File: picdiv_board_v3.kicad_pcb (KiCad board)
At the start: 2 copper layers, 75 x 100 mm, 81 parts, among them J1 DC-Input, J10 PPS_B, J101 MountingHole_M2.5, J102 Conn_Coaxial, J103 Conn_Coaxial, J104 MountingHole_M2.5, J105 Conn_01x06, J106 PPS_A, J107 PPS_A, J14 TEST_1PPS, J4 SYNC, J6 PPS_B, J8 SYNC, Q1 Q_PNP_BEC, Q2 Q_PNP_BEC, SW101 SW_DIP_x03, U101 LT1963AxT-3.3, U102 LT1963AxT-3.3, U103 LT1963AEQ, U104 LTC6993xS6-1, U105 IDT5PB1108, U3 PIC12F675, U6 IDT5PB1108

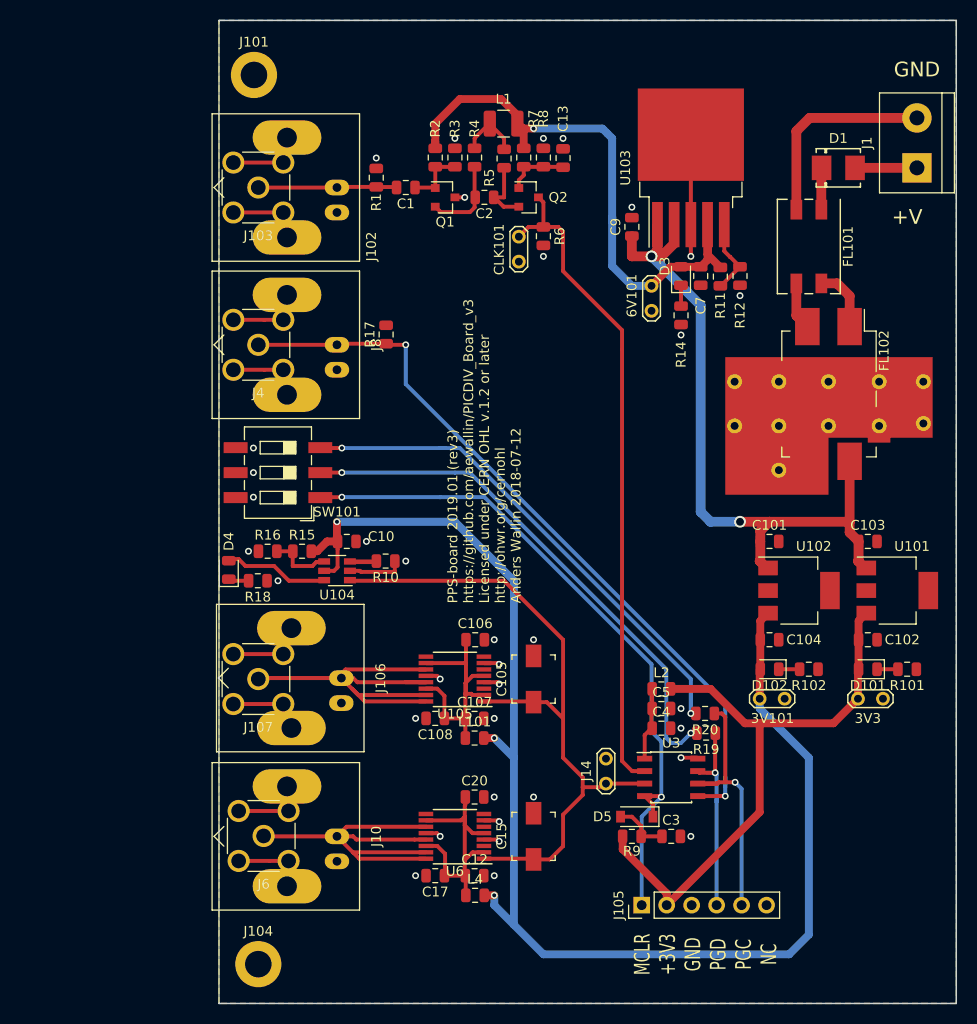
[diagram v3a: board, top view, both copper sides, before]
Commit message: gnd-vias, silk, move PPSB connectors.
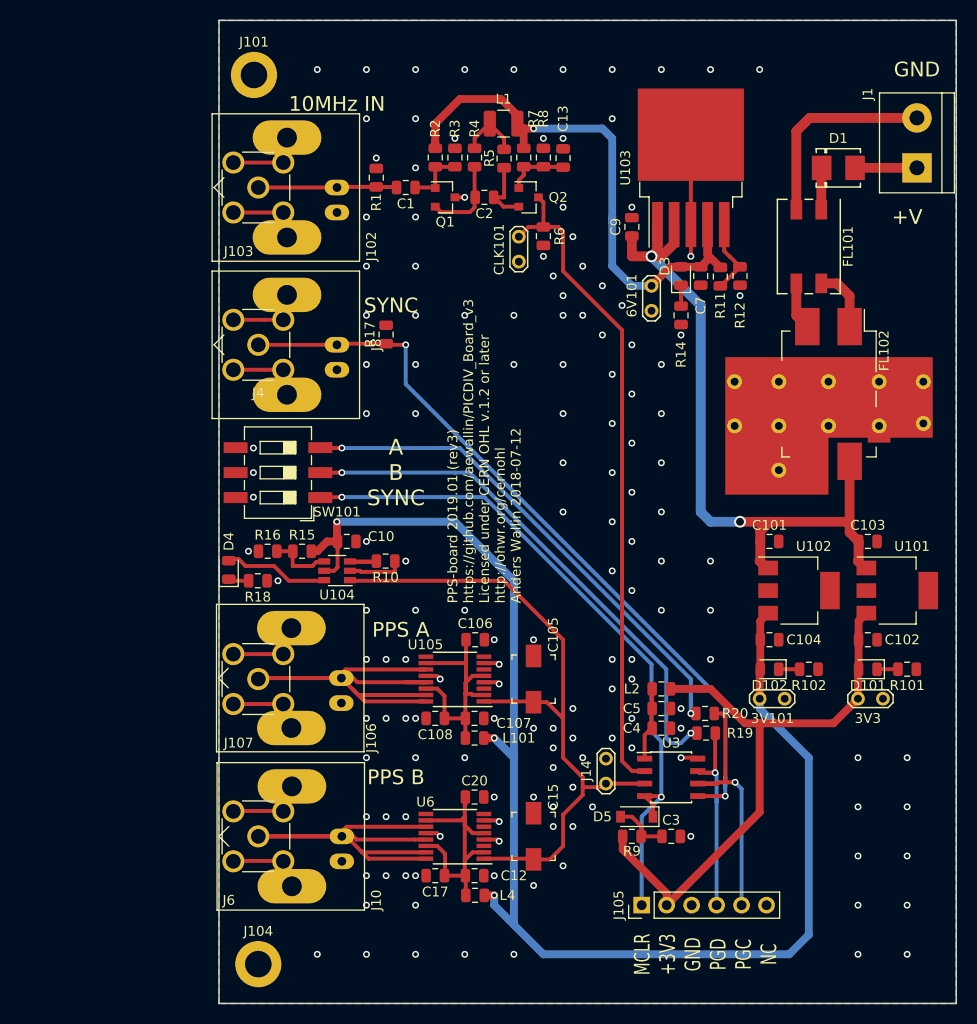
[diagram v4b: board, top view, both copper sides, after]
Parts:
- moved J6 0.54 mm to (129.0, 133.0)
- moved J10 0.50 mm to (137.5, 133.0)
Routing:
- net /PPS_B: track 43.5 -> 50.7 mm
- net GND: vias 35 -> 151
- net (no net): vias 0 -> 1
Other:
- board text added: "10MHz IN"
- board text added: "A B SYNC"
- board text added: "PPS A"
- board text added: "PPS B"
- board text added: "SYNC"

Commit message: minor updates
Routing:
- net GND: vias 151 -> 152
- net (no net): vias 1 -> 0
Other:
- board text added: "DIP Switch: Digikey CKN10901-ND"

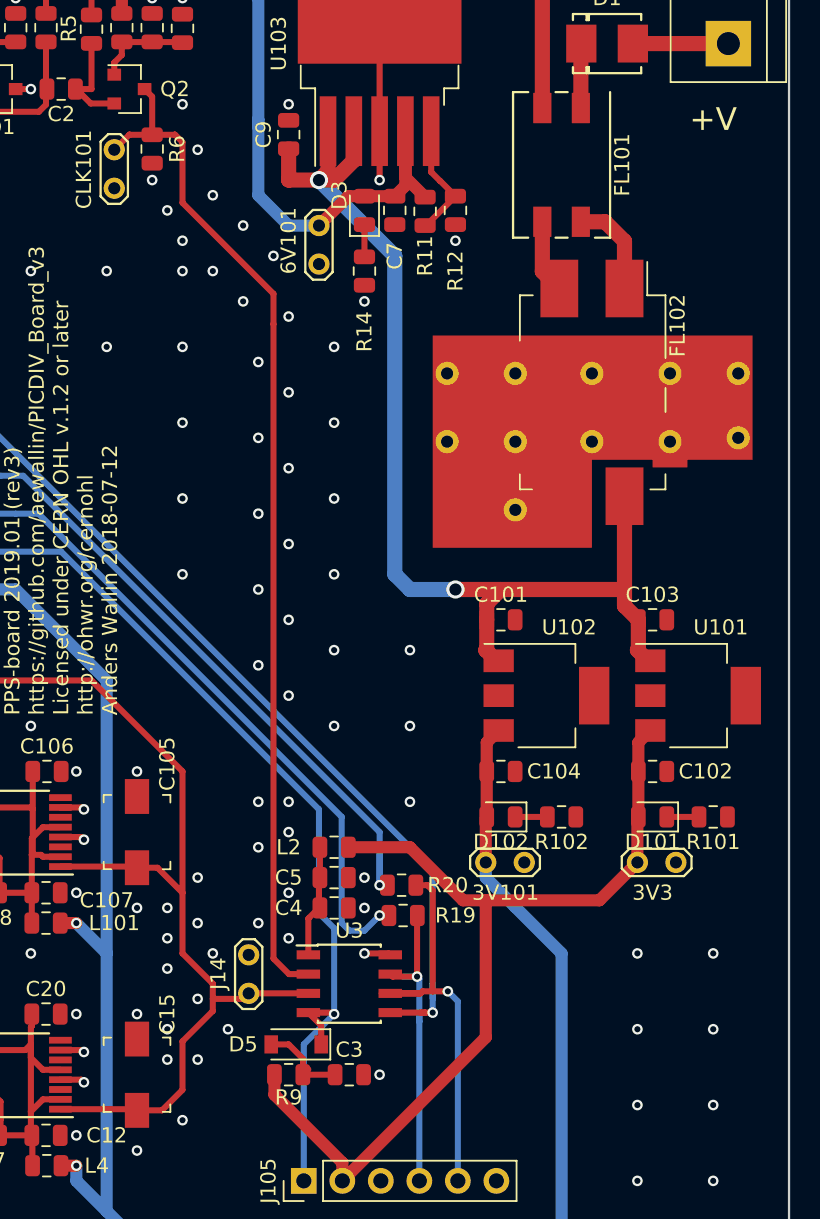
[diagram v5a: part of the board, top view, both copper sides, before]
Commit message: fix missing symbols (kicad lib)
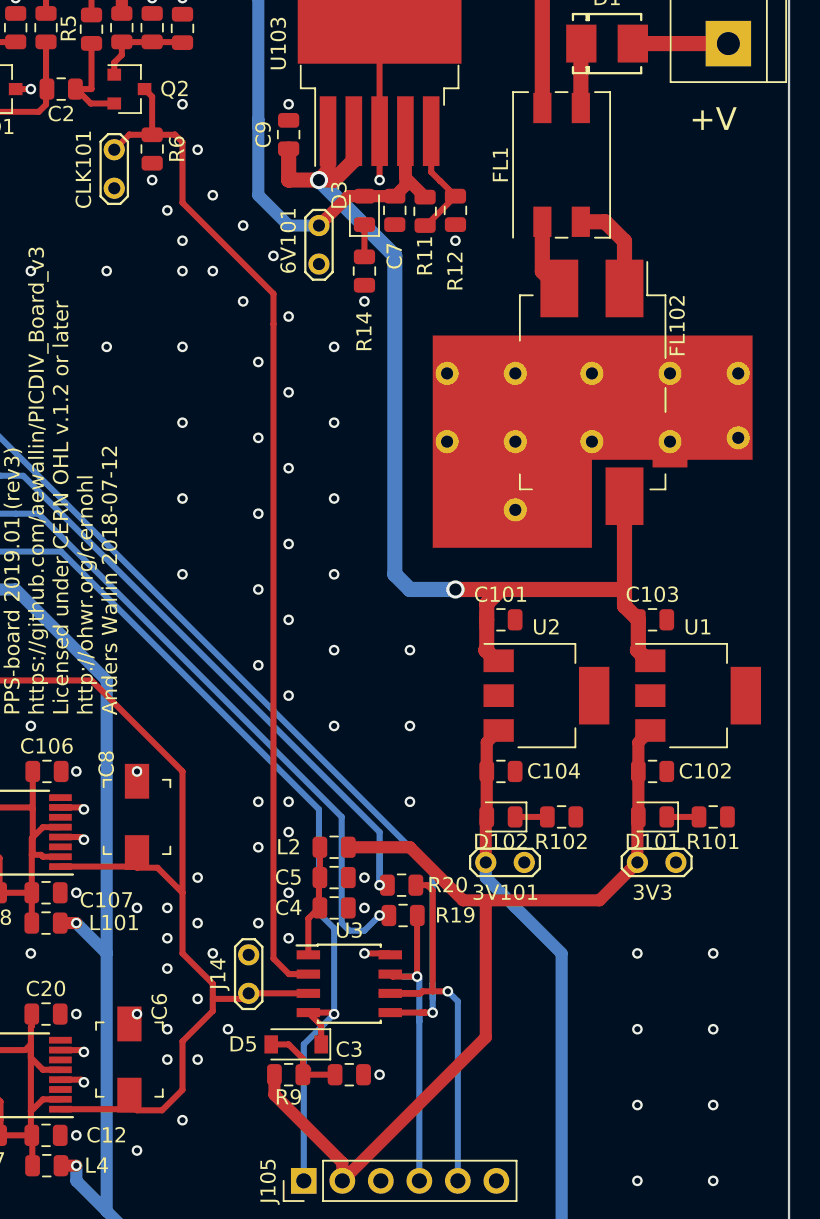
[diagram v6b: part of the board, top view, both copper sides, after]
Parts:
- removed C105, C15: 10p, Capacitor_SMD:C_Trimmer_Murata_TZB4-A
- removed FL101: EMI_Filter_LL_1423, awallinKiCadFootprints:Filter_Bourns_SRF0905_6.0x9.2mm
- removed U101, U102: LT1963AxT-3.3, Package_TO_SOT_SMD:SOT-223-3_TabPin2
- added C6: C_Trim, Capacitor_SMD:C_Trimmer_Murata_TZB4-A, F.Cu at (156.5, 132.0)
- added C8: C_Trim, Capacitor_SMD:C_Trimmer_Murata_TZB4-A, F.Cu at (157.0, 116.0)
- added FL1: Filter_EMI_LL_1423, Filter:Filter_Bourns_SRF0905_6.0x9.2mm, F.Cu at (185.0, 73.0)
- added U1: LT1963AxST-3.3, Package_TO_SOT_SMD:SOT-223-3_TabPin2, F.Cu at (194.0, 108.0)
- added U2: LT1963AxST-3.3, Package_TO_SOT_SMD:SOT-223-3_TabPin2, F.Cu at (184.0, 108.0)

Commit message: kicad6 version
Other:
- net class Default removed
- net class wide removed
